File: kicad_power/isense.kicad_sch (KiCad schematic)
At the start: 14 parts

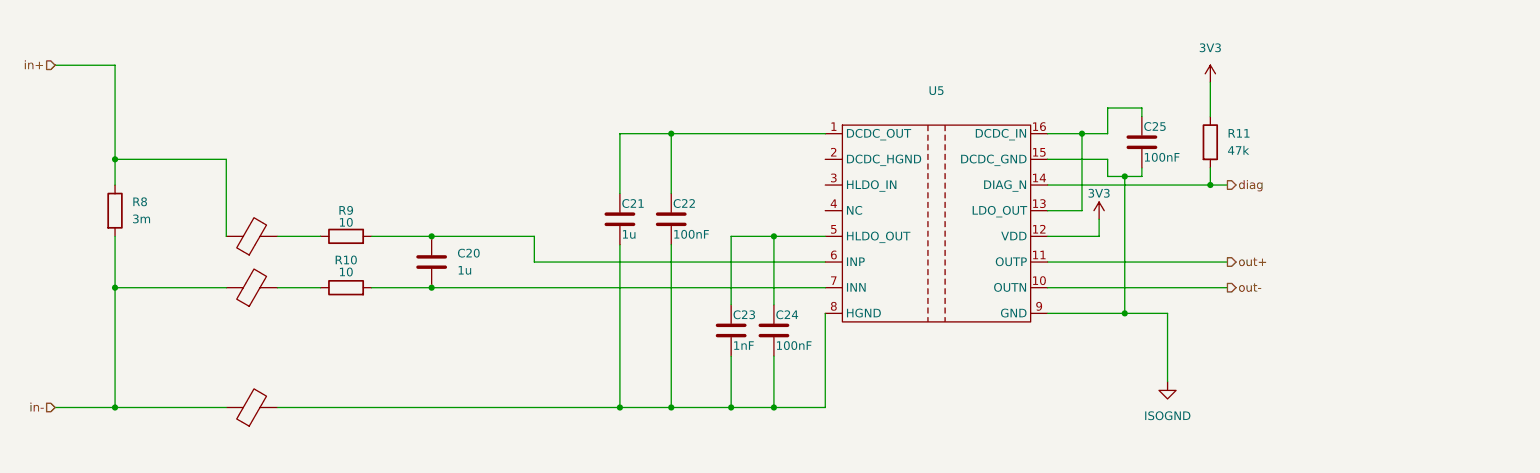
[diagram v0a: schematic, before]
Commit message: finished initial layout of power stage in KiCAD
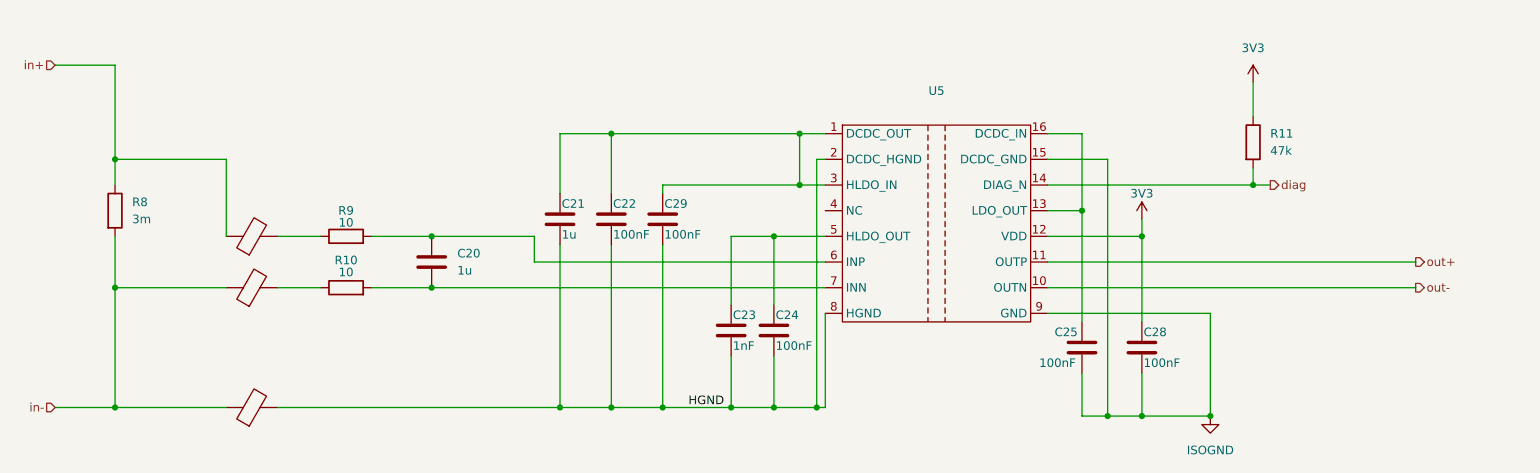
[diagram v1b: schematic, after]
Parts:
- added C28, C29: 100nF, Capacitor_SMD:C_0402_1005Metric, symbol Device:C
- R10, R9: Partno RC0402FR-0710RL -> RC0402JR-0710RL
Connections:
- net 3V3: now also C28.1
- net ISOGND: now also C28.2
- net HGND: now reaches C21.2, C22.2, C23.2, C24.2, FB3.2, U5.8 (HGND)
- net HGND: now also U5.2 (DCDC_HGND), C29.2
- net at C21.1, C22.1, U5.1 (DCDC_OUT): now also U5.3 (HLDO_IN), C29.1
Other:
- moved on the sheet: C21, C22, C25, R11

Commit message: introduced AGND and A3V3, ensures HV design rules
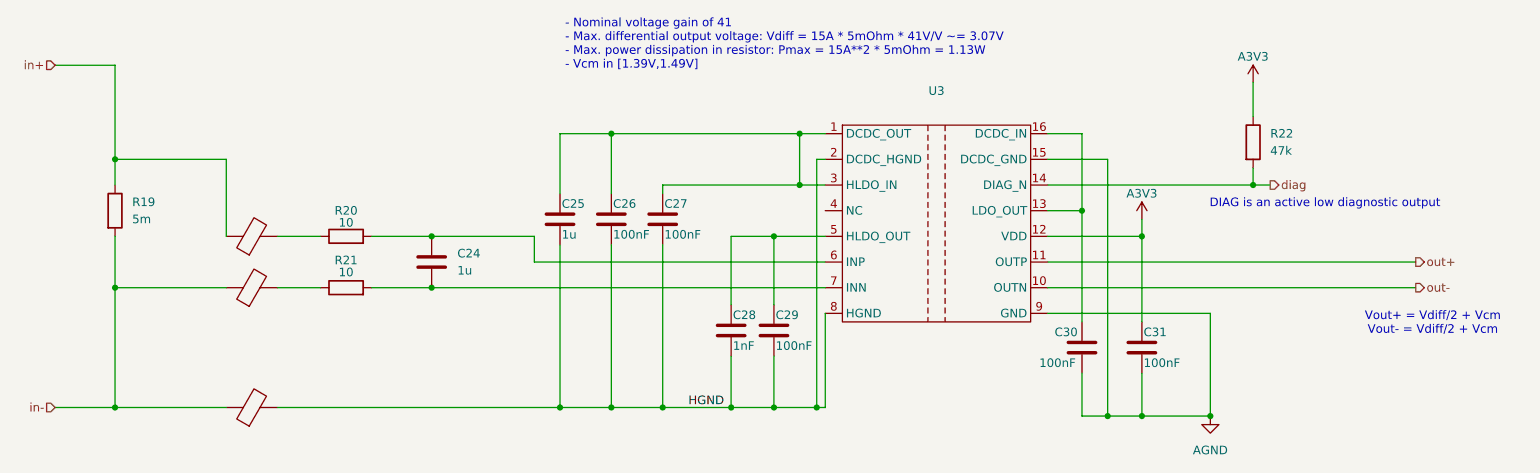
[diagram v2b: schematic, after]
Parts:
- R19: renamed from R8; value 3m -> 5m; Partno CSNL2512FT3L00 -> MCS3264R005FER
- renumbered C20 to C24, C21 to C25, C22 to C26, C29 to C27, C23 to C28, C24 to C29, C25 to C30, C28 to C31, R9 to R20, R10 to R21, R11 to R22, U5 to U3
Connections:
- net 3V3 renamed A3V3
- net ISOGND renamed AGND
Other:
- note added: "- Nominal voltage gain of 41 - Max. differential output voltage: Vdiff = 15A * 5mOhm * 41V/V ~= 3.07V - Max. power dissipation in resistor: Pmax = 15A**2 * 5mOhm = 1.13W - Vcm in [1.39V,1.49V]"
- note added: "DIAG is an active low diagnostic output"
- note added: "Vout+ = Vdiff/2 + Vcm Vout- = Vdiff/2 + Vcm"
- title: (none) -> Current sensing

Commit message: corrected partname of AMC3302DWER
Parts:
- U3: footprint mdriver:PAMC3302DWER -> mdriver:AMC3302DWER; Partno AMC3302 -> AMC3302DWER
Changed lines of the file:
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@@
 			)
 		)
-		(property "Footprint" "mdriver:PAMC3302DWER"
+		(property "Footprint" "mdriver:AMC3302DWER"
 			(at 181.61 85.09 0)
 			(effects
@@
 			)
 		)
-		(property "Partno" "AMC3302"
+		(property "Partno" "AMC3302DWER"
 			(at 181.61 85.09 0)
 			(effects

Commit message: finished version 1.1 of power board
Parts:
- C24, C25: JLCPCB (none) -> C14445
- C26, C27, C29, C30, C31: JLCPCB (none) -> C1525
- C28: JLCPCB (none) -> C1523
- FB1, FB2, FB3: JLCPCB (none) -> C7038862
- R19: JLCPCB (none) -> C108931
- R20, R21: JLCPCB (none) -> C4109
- R22: JLCPCB (none) -> C25563
- U3: JLCPCB (none) -> C4990160
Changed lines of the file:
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@@
 		(title "Current sensing")
 		(date "2025-08-07")
+		(rev "1.1")
 	)
 	(text "DIAG is an active low diagnostic output"
@@
 			)
 		)
+		(property "JLCPCB" "C25563"
+			(at 228.6 74.93 0)
+			(effects
+				(font
+					(size 1.27 1.27)
+				)
+				(hide yes)
+			)
+		)
 		(pin "2"
 		)
@@
 		)
 		(property "Partno" "CL05B102KB5NNNC"
+			(at 151.13 102.87 0)
+			(effects
+				(font
+					(size 1.27 1.27)
+				)
+				(hide yes)
+			)
+		)
+		(property "JLCPCB" "C1523"
 			(at 151.13 102.87 0)
 			(effects
@@
 			)
 		)
+		(property "JLCPCB" "C7038862"
+			(at 80.01 96.52 90)
+			(effects
+				(font
+					(size 1.27 1.27)
+				)
+				(hide yes)
+			)
+		)
 		(pin "2"
 		)
@@
 		)
 		(property "Partno" "C0402C104K4RECAUTO "
+			(at 157.48 102.87 0)
+			(effects
+				(font
+					(size 1.27 1.27)
+				)
+				(hide yes)
+			)
+		)
+		(property "JLCPCB" "C1525"
 			(at 157.48 102.87 0)
 			(effects
@@
 			)
 		)
+		(property "JLCPCB" "C7038862"
+			(at 80.01 88.9 90)
+			(effects
+				(font
+					(size 1.27 1.27)
+				)
+				(hide yes)
+			)
+		)
 		(pin "2"
 		)
@@
 			)
 		)
+		(property "JLCPCB" "C1525"
+			(at 212.09 105.41 0)
+			(effects
+				(font
+					(size 1.27 1.27)
+				)
+				(hide yes)
+			)
+		)
 		(pin "1"
 		)
@@
 			)
 		)
+		(property "JLCPCB" "C1525"
+			(at 133.35 86.36 0)
+			(effects
+				(font
+					(size 1.27 1.27)
+				)
+				(hide yes)
+			)
+		)
 		(pin "1"
 		)
@@
 		)
 		(property "Partno" "C0402C104K4RECAUTO "
+			(at 140.97 86.36 0)
+			(effects
+				(font
+					(size 1.27 1.27)
+				)
+				(hide yes)
+			)
+		)
+		(property "JLCPCB" "C1525"
 			(at 140.97 86.36 0)
 			(effects
@@
 			)
 		)
+		(property "JLCPCB" "C14445"
+			(at 106.68 92.71 0)
+			(effects
+				(font
+					(size 1.27 1.27)
+				)
+				(hide yes)
+			)
+		)
 		(pin "1"
 		)
@@
 			)
 		)
+		(property "JLCPCB" "C4109"
+			(at 93.98 88.9 90)
+			(effects
+				(font
+					(size 1.27 1.27)
+				)
+				(hide yes)
+			)
+		)
 		(pin "2"
 		)
@@
 		)
 		(property "Partno" "RC0402JR-0710RL"
+			(at 93.98 96.52 90)
+			(effects
+				(font
+					(size 1.27 1.27)
+				)
+				(hide yes)
+			)
+		)
+		(property "JLCPCB" "C4109"
 			(at 93.98 96.52 90)
 			(effects
@@
 			)
 		)
+		(property "JLCPCB" "C7038862"
+			(at 80.01 114.3 90)
+			(effects
+				(font
+					(size 1.27 1.27)
+				)
+				(hide yes)
+			)
+		)
 		(pin "2"
 		)
@@
 		)
 		(property "Partno" "C0402C104K4RECAUTO "
+			(at 203.2 105.41 0)
+			(effects
+				(font
+					(size 1.27 1.27)
+				)
+				(hide yes)
+			)
+		)
+		(property "JLCPCB" "C1525"
 			(at 203.2 105.41 0)
 			(effects
@@
 			)
 		)
+		(property "JLCPCB" "C108931"
+			(at 59.69 85.09 0)
+			(effects
+				(font
+					(size 1.27 1.27)
+				)
+				(hide yes)
+			)
+		)
 		(pin "2"
 		)
@@
 			)
 		)
+		(property "JLCPCB" "C4990160"
+			(at 181.61 85.09 0)
+			(effects
+				(font
+					(size 1.27 1.27)
+				)
+				(hide yes)
+			)
+		)
 		(pin "7"
 		)
@@
 			(at 125.73 86.36 0)
 			(effects
+				(font
+					(size 1.27 1.27)
+				)
+				(hide yes)
+			)
+		)
+		(property "JLCPCB" "C14445"
+			(at 125.73 86.36 0)
+			(effects
